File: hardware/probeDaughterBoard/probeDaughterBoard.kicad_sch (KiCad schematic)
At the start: 44 parts, among them J1 Conn_02x04_Odd_Even, J2 Conn_01x03_Socket, J3 Conn_01x02_Socket, J4 Conn_01x06

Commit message: basic sensor setup
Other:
- note added: "0"
- note added: "VERF should be AIN3"
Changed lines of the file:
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@@
+    (stroke (width 0) (type default))
+  )
+  (polyline (pts (xy 86.995 20.955) (xy 90.17 19.685))
     (stroke (width 0) (type default))
   )
@@
     (stroke (width 0) (type default))
   )
+  (text "VERF should be AIN3" (at 121.92 35.56 0)
+    (effects (font (size 1.27 1.27)) (justify left bottom))
+  )
+  (text "0" (at 92.075 21.59 0)
+    (effects (font (size 1.27 1.27)) (justify left bottom))
+  )
   (text " Non-Inverting op-amp Gain 3.2" (at 57.785 21.59 0)

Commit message: bugfix adc
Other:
- note added: "12K"
- note added: "2.2K"
- note added: "INT is active Low, flip led"
- note added: "J1 is flipped"
- note added: "Ofset by 0.512V"
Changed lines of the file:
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@@
+    (stroke (width 0) (type default))
+  )
+  (polyline (pts (xy 36.83 40.64) (xy 40.005 39.37))
     (stroke (width 0) (type default))
   )
@@
     (stroke (width 0) (type default))
   )
+  (polyline (pts (xy 29.845 46.99) (xy 33.02 45.72))
+    (stroke (width 0) (type default))
+  )
   (wire (pts (xy 175.26 21.59) (xy 169.545 21.59))
     (stroke (width 0) (type default))
@@
     (stroke (width 0) (type default))
   )
+  (polyline (pts (xy 29.845 45.72) (xy 33.02 46.99))
+    (stroke (width 0) (type default))
+  )
   (polyline (pts (xy 86.995 20.955) (xy 90.17 19.685))
     (stroke (width 0) (type default))
@@
     (stroke (width 0) (type default))
   )
+  (polyline (pts (xy 19.685 41.91) (xy 33.02 41.91))
+    (stroke (width 0) (type default))
+  )
   (wire (pts (xy 85.09 175.895) (xy 84.455 175.895))
     (stroke (width 0) (type default))
@@
     (stroke (width 0) (type default))
   )
+  (polyline (pts (xy 36.83 39.37) (xy 40.005 40.64))
+    (stroke (width 0) (type default))
+  )
   (wire (pts (xy 36.195 179.705) (xy 36.195 180.975))
     (stroke (width 0) (type default))
@@
     (stroke (width 0) (type default))
   )
+  (text "Ofset by 0.512V" (at 13.97 46.355 0)
+    (effects (font (size 1.27 1.27)) (justify left bottom))
+  )
+  (text "INT is active Low, flip led" (at 172.085 67.945 0)
+    (effects (font (size 1.27 1.27)) (justify left bottom))
+  )
   (text "VERF should be AIN3" (at 121.92 35.56 0)
     (effects (font (size 1.27 1.27)) (justify left bottom))
@@
     (effects (font (size 1.27 1.27)) (justify left bottom))
   )
+  (text "12K" (at 40.005 38.1 0)
+    (effects (font (size 1.27 1.27)) (justify left bottom))
+  )
+  (text "2.2K" (at 27.94 49.53 0)
+    (effects (font (size 1.27 1.27)) (justify left bottom))
+  )
+  (text "J1 is flipped" (at 233.045 59.055 0)
+    (effects (font (size 1.27 1.27)) (justify left bottom))
+  )

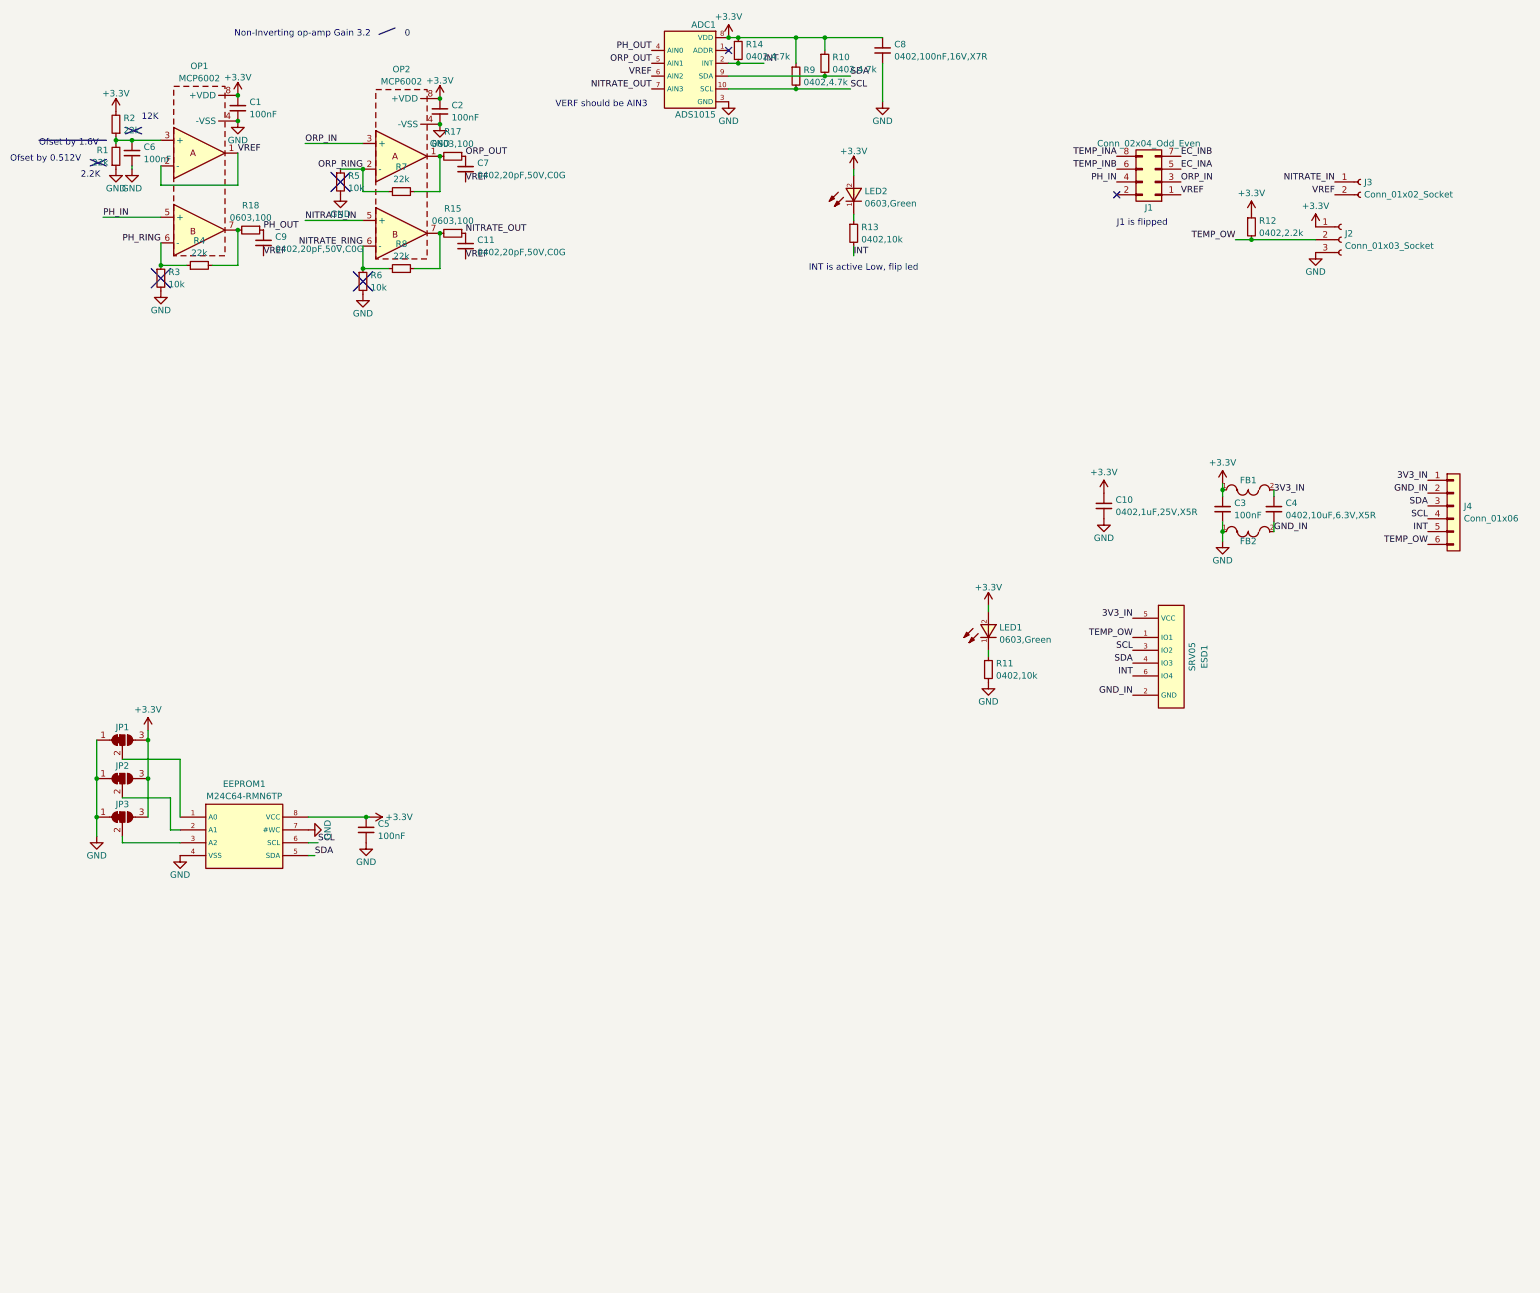
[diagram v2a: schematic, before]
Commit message: -added CAD models -moved to KiCAD 8.0 -clang formatting -rebuild sensor calibration -add logging and analytics file -added adaptive backlight -added work hours for gps sync
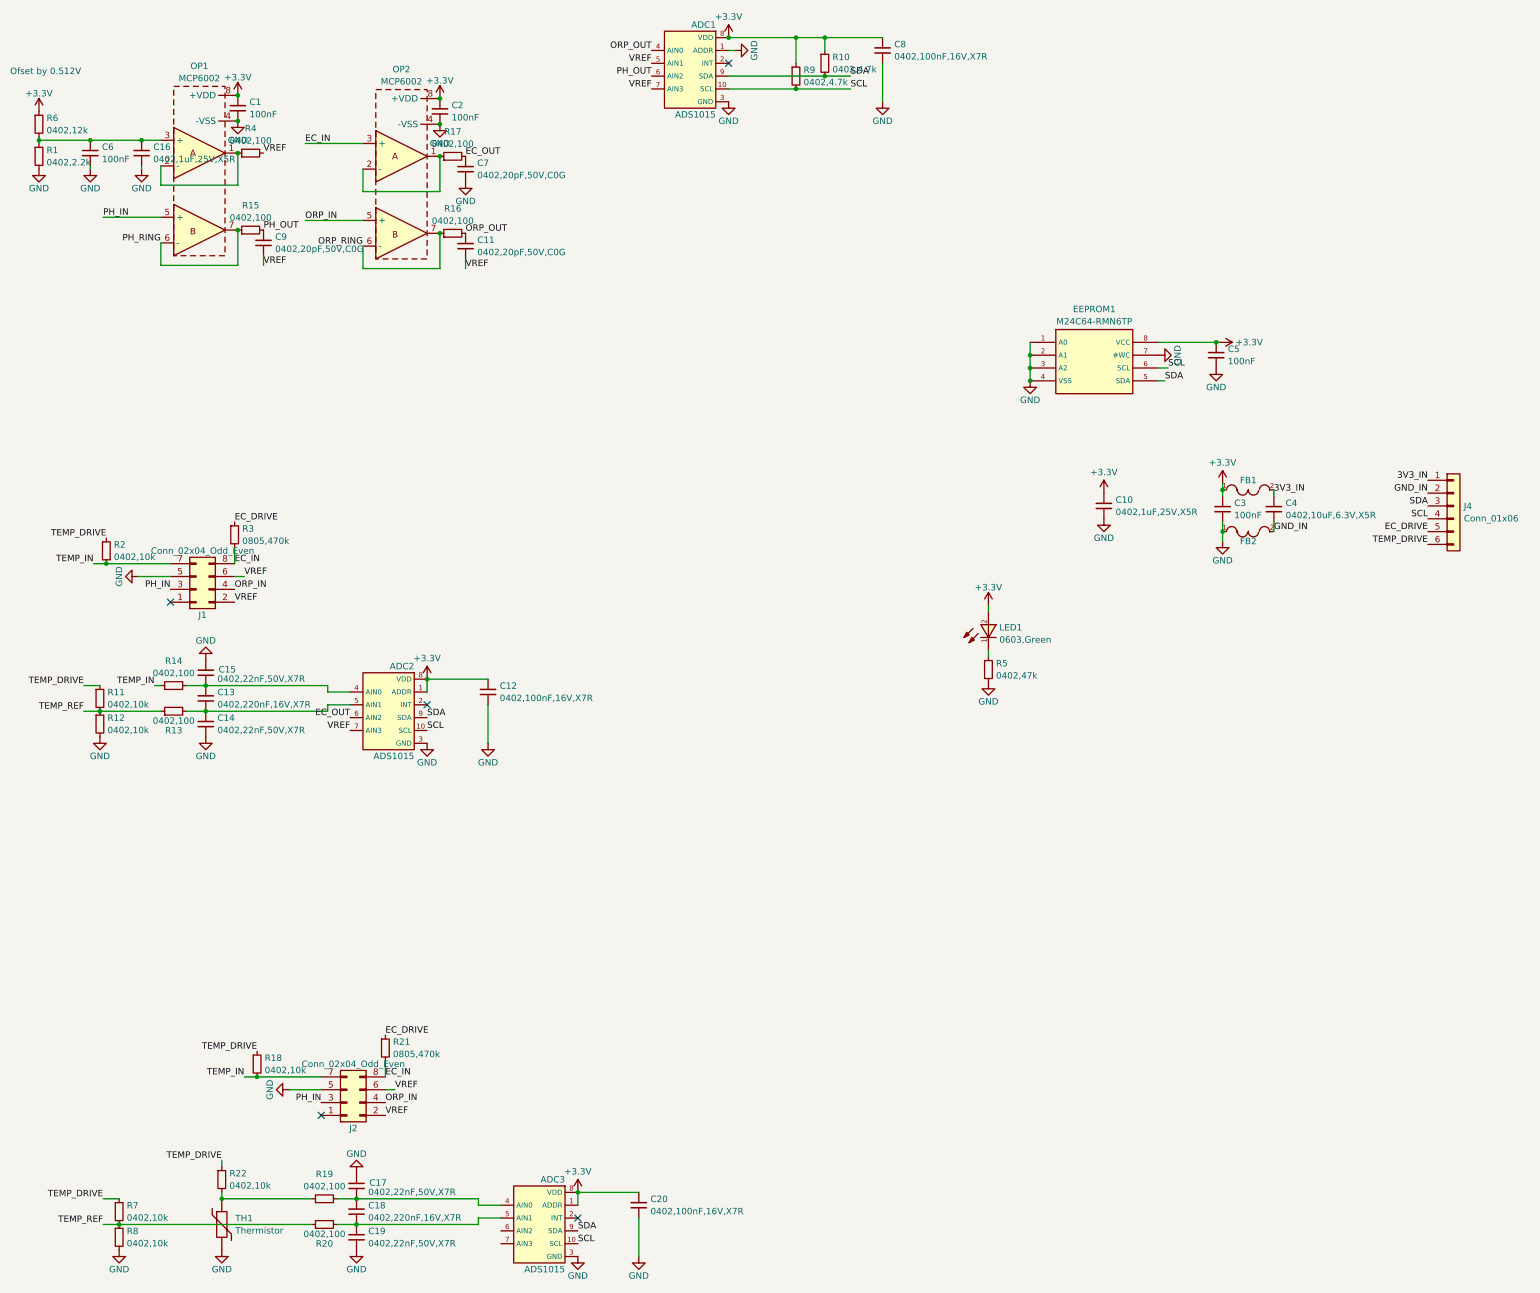
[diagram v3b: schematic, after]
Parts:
- removed ESD1: SRV05, footprint:SOT-23-6_L2.9-W1.6-P0.95-LS2.8-BR, symbol jlcpcb-diodes:SRV05
- removed J2: Conn_01x03_Socket, Connector_Wire:SolderWire-0.5sqmm_1x03_P4.6mm_D0.9mm_OD2.1mm_Relief, symbol Connector:Conn_01x03_Socket
- removed J3: Conn_01x02_Socket, Connector_Wire:SolderWire-0.5sqmm_1x02_P4.6mm_D0.9mm_OD2.1mm_Relief, symbol Connector:Conn_01x02_Socket
- removed JP1, JP2, JP3: SolderJumper_3_Bridged12, Jumper:SolderJumper-3_P1.3mm_Bridged12_RoundedPad1.0x1.5mm_NumberLabels, symbol Jumper:SolderJumper_3_Bridged12
- removed LED2: 0603,Green, footprint:LED0603, symbol jlcpcb-diodes:0603,Green
- removed R1, R2, R4, R7, R8: 22k, footprint:0603_1608Metric, symbol jlcpcb-basic-resistor:0603,22k
- removed R12: 0402,2.2k, footprint:0402_1005Metric, symbol jlcpcb-basic-resistor:0402,2.2k
- removed R13: 0402,10k, footprint:0402_1005Metric, symbol jlcpcb-basic-resistor:0402,10k
- removed R14: 0402,4.7k, footprint:0402_1005Metric, symbol jlcpcb-basic-resistor:0402,4.7k
- removed R15, R17, R18: 0603,100, footprint:0603_1608Metric, symbol jlcpcb-basic-resistor:0603,100
- removed R3, R5, R6: 10k, footprint:0603_1608Metric, symbol jlcpcb-basic-resistor:0603,10k
- added ADC2, ADC3: ADS1015, footprint:MSOP-10_L3.0-W3.0-P0.50-LS5.0-BL, symbol jlcpcb-extended:ADS1115IDGSR
- added C12, C20: 0402,100nF,16V,X7R, footprint:0402_1005Metric, symbol jlcpcb-basic-capacitor:0402,100nF,16V,X7R
- added C13, C18: 0402,220nF,16V,X7R, footprint:0402_1005Metric, symbol jlcpcb-basic-capacitor:0402,220nF,16V,X7R
- added C14, C15, C17, C19: 0402,22nF,50V,X7R, footprint:0402_1005Metric, symbol jlcpcb-basic-capacitor:0402,22nF,50V,X7R
- added C16: 0402,1uF,25V,X5R, footprint:0402_1005Metric, symbol jlcpcb-basic-capacitor:0402,1uF,25V,X5R
- added J2: Conn_02x04_Odd_Even, Connector_PinHeader_2.00mm:PinHeader_2x04_P2.00mm_Horizontal, symbol Connector_Generic:Conn_02x04_Odd_Even
- added R1: 0402,2.2k, footprint:0402_1005Metric, symbol jlcpcb-basic-resistor:0402,2.2k
- added R12, R18, R2, R22, R7, R8: 0402,10k, footprint:0402_1005Metric, symbol jlcpcb-basic-resistor:0402,10k
- added R13, R14, R15, R16, R17, R19, R20, R4: 0402,100, footprint:0402_1005Metric, symbol jlcpcb-basic-resistor:0402,100
- added R21, R3: 0805,470k, footprint:0805_2012Metric, symbol jlcpcb-basic-resistor:0805,470k
- added R5: 0402,47k, footprint:0402_1005Metric, symbol jlcpcb-basic-resistor:0402,47k
- added R6: 0402,12k, footprint:0402_1005Metric, symbol jlcpcb-basic-resistor:0402,12k
- added TH1: Thermistor, symbol Device:Thermistor
- C10: value 0402,1uF,25V,X5R -> 0402,1uF,25V,X5R
- C11, C7, C9: value 0402,20pF,50V,C0G -> 0402,20pF,50V,C0G
- C4: value 0402,10uF,6.3V,X5R -> 0402,10uF,6.3V,X5R
- C8: value 0402,100nF,16V,X7R -> 0402,100nF,16V,X7R
- J4: footprint Connector_Wire:SolderWire-0.1sqmm_1x06_P3.6mm_D0.4mm_OD1mm_Relief -> Connector_Wire:SolderWire-0.1sqmm_1x06_P3.6mm_D0.4mm_OD1mm
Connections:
- net EC_INA is gone; now on net GND: J1.5 (Pin_5)
- net NITRATE_IN is gone; now on net ORP_IN: OP2.5 (+)
- net NITRATE_RING is gone; now on net ORP_RING: OP2.6 (-)
- net TEMP_INB is gone; now on net VREF: J1.6 (Pin_6)
- net +3.3V: now also ADC2.1 (ADDR), ADC2.8 (VDD), ADC3.1 (ADDR), ADC3.8 (VDD), C12.1, C20.1, R6.1
- net GND: now also ADC1.1 (ADDR), C7.2, EEPROM1.1 (A0), EEPROM1.2 (A1), EEPROM1.3 (A2), ADC2.3 (GND), ADC3.3 (GND), C12.2, C14.2, C15.1, C16.2, C17.1, C19.2, C20.2, J2.5 (Pin_5), R1.2, R12.2, R5.2, R8.2, TH1.2; no longer R11.2
- net ORP_IN: now also J1.4 (Pin_4), J2.4 (Pin_4); no longer J1.3 (Pin_3), OP2.3 (+)
- net ORP_OUT: now also ADC1.4 (AIN0), C11.1, R16.2; no longer ADC1.5 (AIN1), C7.1
- net ORP_RING: now also OP2.7, R16.1; no longer OP2.2 (-)
- net PH_IN: now also J1.3 (Pin_3), J2.3 (Pin_3); no longer J1.4 (Pin_4)
- net PH_OUT: now also ADC1.6 (AIN2), R15.2; no longer ADC1.4 (AIN0)
- net PH_RING: now also OP1.7, R15.1
- net SCL: now also ADC2.10 (SCL), ADC3.10 (SCL)
- net SDA: now also ADC2.9 (SDA), ADC3.9 (SDA)
- net VREF: now also ADC1.5 (AIN1), ADC1.7 (AIN3), J1.2 (Pin_2), ADC2.7 (AIN3), J2.2 (Pin_2), J2.6 (Pin_6), R4.2; no longer ADC1.6 (AIN2), C7.2, J1.1 (Pin_1), OP1.1, OP1.2 (-)
- net at C6.1, OP1.3 (+): now also C16.1, R1.1, R6.2
- net at OP2.1: now also OP2.2 (-), R17.1
- net at LED1.1 (C): now also R5.1; no longer R11.1
- net EC_INB renamed TEMP_IN
- net TEMP_IN: now also J2.7 (Pin_7), R14.1, R18.2, R2.2
- net INT: no longer names the net of ADC1.2 (INT)
- net INT: no longer J4.5 (Pin_5)
- removed net NITRATE_OUT: ADC1.7 (AIN3), C11.1
- net TEMP_INA renamed EC_IN
- net EC_IN: now also OP2.3 (+), J2.8 (Pin_8), R21.2, R3.2
- net TEMP_OW renamed TEMP_DRIVE
- net TEMP_DRIVE: now also R11.1, R18.1, R2.1, R22.1, R7.1
- new net: ADC3.4 (AIN0), C17.2, C18.1, R19.2
- new net: ADC3.5 (AIN1), C18.2, C19.1, R20.2
- new net: R19.1, R22.2, TH1.1
- new net: ADC2.4 (AIN0), C13.1, C15.2, R14.2
- new net: OP1.1, OP1.2 (-), R4.1
- new net: ADC2.5 (AIN1), C13.2, C14.1, R13.2
- new net EC_DRIVE: J4.5 (Pin_5), R21.1, R3.1
- new net EC_OUT: ADC2.6 (AIN2), C7.1, R17.2
- new net TEMP_REF: R11.2, R12.1, R13.1, R20.1, R7.2, R8.1
- no-connect marks 2 -> 5
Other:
- note removed: "0"
- note removed: "12K"
- note removed: "2.2K"
- note removed: "INT is active Low, flip led"
- note removed: "J1 is flipped"
- note removed: "Non-Inverting op-amp Gain 3.2"
- note removed: "Ofset by 1.6V"
- note removed: "VERF should be AIN3"
- moved on the sheet: C5, C6, EEPROM1, J1
